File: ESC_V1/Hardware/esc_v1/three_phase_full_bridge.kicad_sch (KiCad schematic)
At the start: 7 parts, among them Q1 IRFH7084TRPBF, Q2 IRFH7084TRPBF, Q3 IRFH7084TRPBF, Q4 IRFH7084TRPBF, Q5 IRFH7084TRPBF, Q6 IRFH7084TRPBF

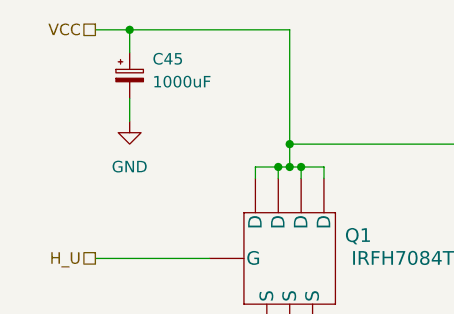
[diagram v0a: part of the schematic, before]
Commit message: Components roughly placed in layout
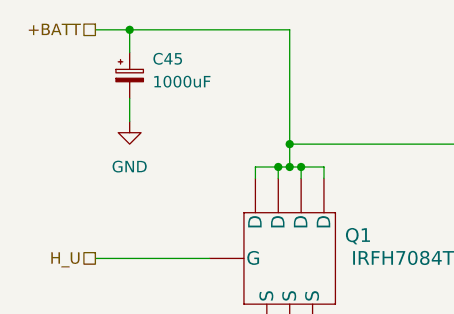
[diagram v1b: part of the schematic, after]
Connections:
- net VCC renamed +BATT
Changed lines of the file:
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@@
     (effects (font (size 1.27 1.27)) (justify right))
   )
-  (hierarchical_label "VCC" (shape passive) (at 76.2 63.5 180)
+  (hierarchical_label "+BATT" (shape passive) (at 76.2 63.5 180)
     (effects (font (size 1.27 1.27)) (justify right))
   )
